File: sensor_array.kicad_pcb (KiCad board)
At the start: 2 copper layers, 125 x 45 mm, 25 parts, among them P1 CONN_01X10, U1 LTV-817, U2 LTV-817, U3 LTV-817, U4 LTV-817, U5 LTV-817, U6 LTV-817, U7 LTV-817, U8 LTV-817

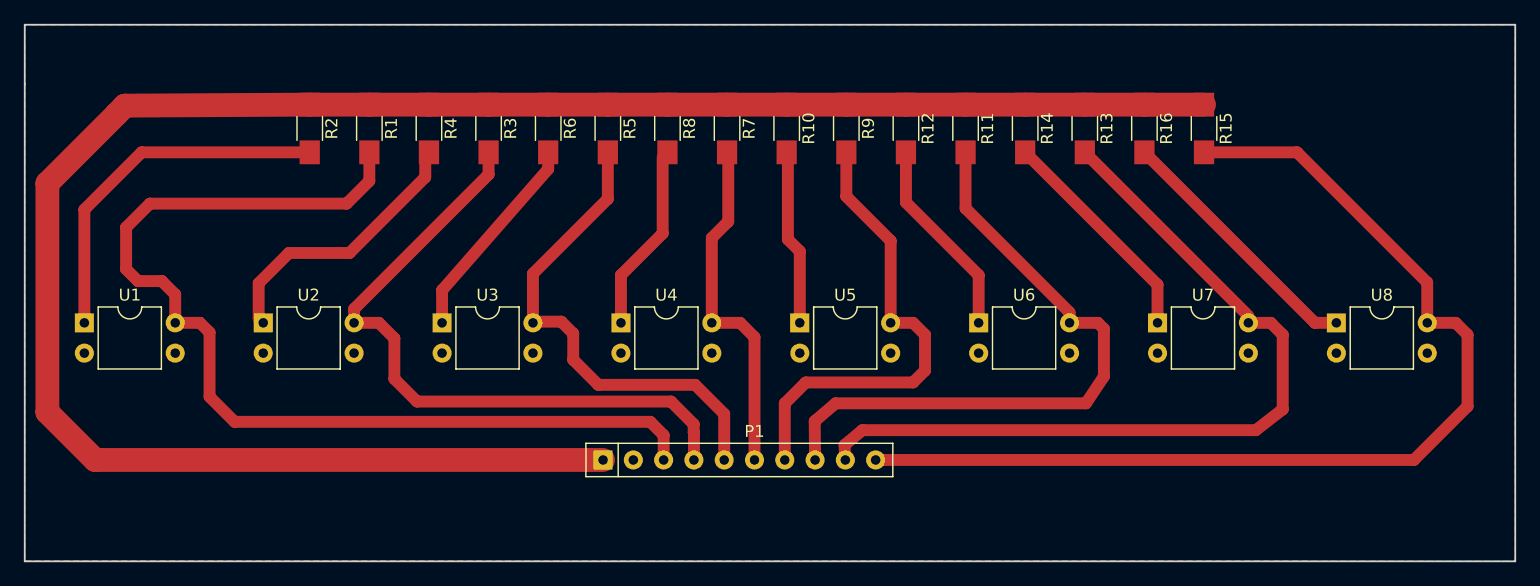
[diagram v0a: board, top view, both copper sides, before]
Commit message: Change resistors to THT
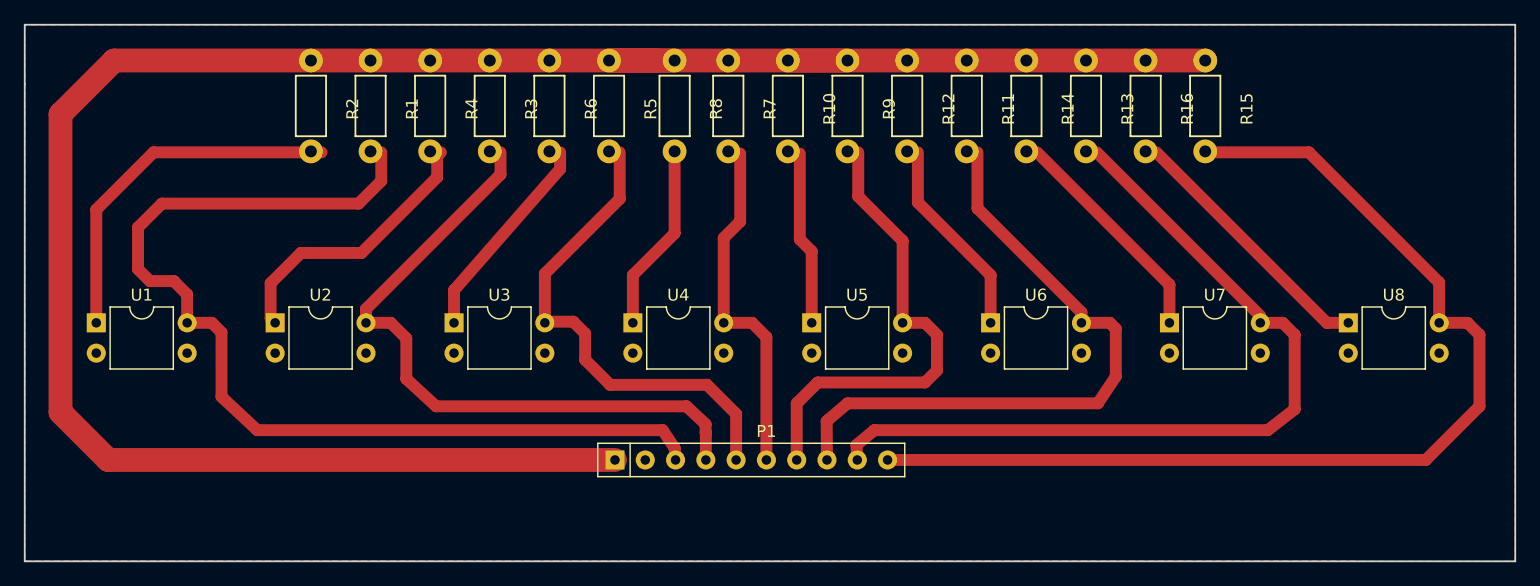
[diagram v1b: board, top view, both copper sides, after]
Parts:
- R1, R10, R11, R12, R13, R14, R15, R16, R2, R3, R4, R5, R6, R7, R8, R9: footprint Resistors_SMD:R_1206_HandSoldering -> Resistors_THT:Resistor_Horizontal_RM7mm
- moved R8 5.73 mm to (169.5, 88.0)
- moved R1 5.70 mm to (144.0, 88.0)
- moved R10 5.70 mm to (179.0, 88.0)
- moved R11 5.70 mm to (194.0, 88.0)
- moved R12 5.70 mm to (189.0, 88.0)
- moved R13 5.70 mm to (204.0, 88.0)
- moved R14 5.70 mm to (199.0, 88.0)
- moved R15 5.70 mm to (214.0, 88.0)
- moved R16 5.70 mm to (209.0, 88.0)
- moved R2 5.70 mm to (139.0, 88.0)
- moved R3 5.70 mm to (154.0, 88.0)
- moved R4 5.70 mm to (149.0, 88.0)
- moved R5 5.70 mm to (164.0, 88.0)
- moved R6 5.70 mm to (159.0, 88.0)
- moved R7 5.70 mm to (174.0, 88.0)
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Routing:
- net +5V: track 167.2 -> 185.5 mm
- net Net-(P1-Pad3): track 85.4 -> 84.8 mm
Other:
- net class Default: clearance 0.2 -> 0.5
- rule trace_clearance: 0.2 -> 0.5

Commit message: Create and add footprint to sensor TCRT5000.
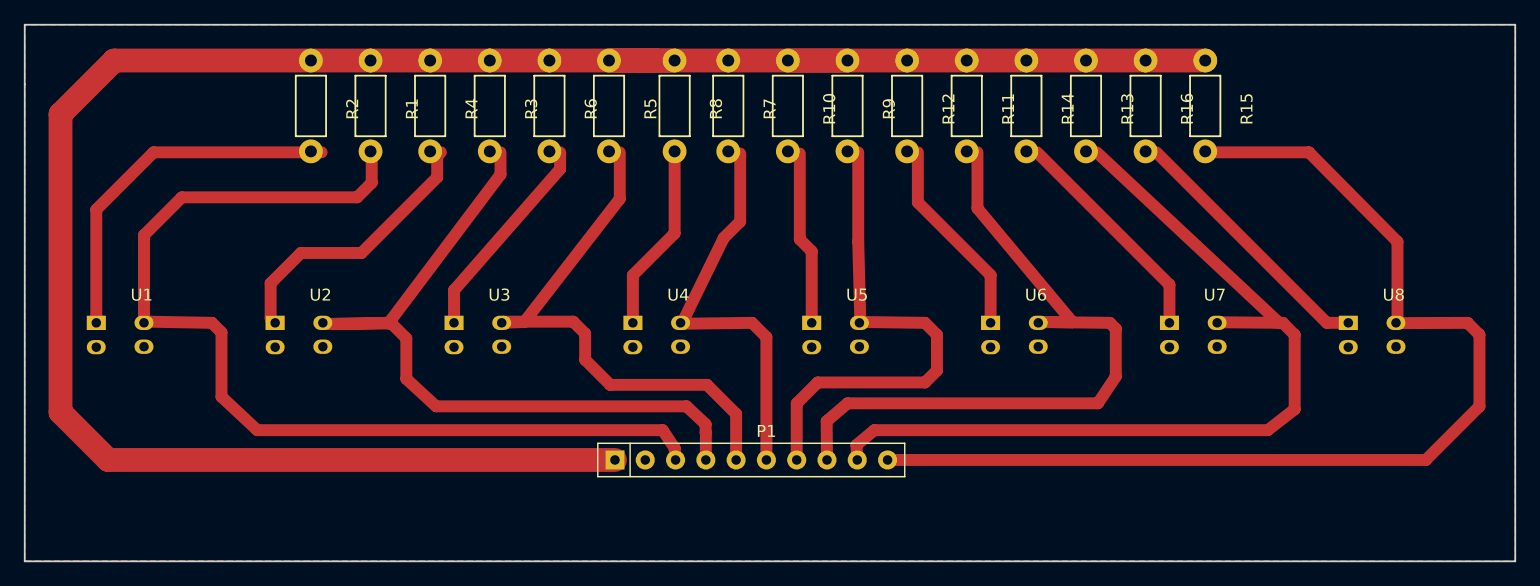
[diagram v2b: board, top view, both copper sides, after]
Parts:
- U1, U2, U3, U4, U5, U6, U7, U8: footprint Housings_DIP:DIP-4_W7.62mm -> my:DIP-4_W7.62mm
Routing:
- net Net-(P1-Pad9): track 68.6 -> 78.3 mm
- net Net-(P1-Pad4): track 55.9 -> 63.6 mm
- net Net-(P1-Pad8): track 54.3 -> 60.2 mm
- net Net-(P1-Pad5): track 41.3 -> 46.8 mm
- net Net-(P1-Pad6): track 29.3 -> 33.7 mm
- net Net-(P1-Pad10): track 87.9 -> 90.0 mm
- net Net-(P1-Pad7): track 39.8 -> 41.7 mm
- net Net-(P1-Pad3): track 84.8 -> 83.9 mm
